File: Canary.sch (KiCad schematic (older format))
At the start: 36 parts, among them J1 CONN_ARM_CM_JTAG_SWD_10, J2 BMD-300-A-R, J3 20021311-00010T4LF, Q1 PMN30UNX, Q2 PMN42XPEAH, Q3 PMN30UNX, SW1 TL3301SPF160QJ, U1 DNP, U2 SHTC3, U3 SGP40, Y1 32.7680 kHz

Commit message: Clean up schem, wire in button
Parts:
- added C26: 0.1u, JetkovKiCADLib:C_0402_NoSilk, symbol Device:C
- added R28: 10k, JetkovKiCADLib:R_0402_NoSilk, symbol Device:R
- added R29: 100k, JetkovKiCADLib:R_0402_NoSilk, symbol Device:R
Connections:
- net labels added: BUTTON
- wire segments 115 -> 127
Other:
- note added: "Button"
- note added: "GPIO Specifications\nVmin = -0.3V, Vmax = VCC+0.3V = 3.9V\nVih = 0.7 * VCC = 2.31V\nVil = 0.3 * VCC = 0.99V"
- note added: "TODO\n- Jellybean BOM\n- Review"
- note removed: "TODO\n- Jellybean BOM\n- Review\n- Button"
- moved on the sheet: C4, J1, U1

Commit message: Spec LED resistors
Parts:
- R10: value ? -> 500R
- R28: value 10k -> 100k
- R8, R9: value ? -> 470R
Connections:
- wire segments 127 -> 132
- no-connect marks 4 -> 9
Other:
- note added: "Vf @ 3mA = 1.8V\nIntensity = 20 mcd"
- note added: "Vf @ 3mA = 1.9V\nIntensity = 20 mcd"
- note added: "Vf @ 3mA = 1.9V\nIntensity = 8 mcd"
- moved on the sheet: C5, Y1
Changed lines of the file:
@@
 L Device:Crystal Y1
 U 1 1 6032C351
-P 5300 1550
-F 0 "Y1" H 5600 1650 50  0000 C CNN
-F 1 "32.7680 kHz" H 5800 1550 50  0000 C CNN
-F 2 "JetkovKiCADLib:FC135327680KAAC3" H 5300 1550 50  0001 C CNN
-F 3 "https://support.epson.biz/td/api/doc_check.php?dl=brief_FC-135&lang=en" H 5300 1550 50  0001 C CNN
-F 4 "CRYSTAL 32.7680KHZ 9PF SMD" H 5300 1550 50  0001 C CNN "Description"
-F 5 "EPSON" H 5300 1550 50  0001 C CNN "Manufacturer"
-F 6 "FC-135 32.7680KA-AC3" H 5300 1550 50  0001 C CNN "Part Number"
-F 7 "-40°C +85°C" H 5300 1550 50  0001 C CNN "Temp Range"
-	1    5300 1550
+P 5350 1550
+F 0 "Y1" H 5650 1650 50  0000 C CNN
+F 1 "32.7680 kHz" H 5850 1550 50  0000 C CNN
+F 2 "JetkovKiCADLib:FC135327680KAAC3" H 5350 1550 50  0001 C CNN
+F 3 "https://support.epson.biz/td/api/doc_check.php?dl=brief_FC-135&lang=en" H 5350 1550 50  0001 C CNN
+F 4 "CRYSTAL 32.7680KHZ 9PF SMD" H 5350 1550 50  0001 C CNN "Description"
+F 5 "EPSON" H 5350 1550 50  0001 C CNN "Manufacturer"
+F 6 "FC-135 32.7680KA-AC3" H 5350 1550 50  0001 C CNN "Part Number"
+F 7 "-40°C +85°C" H 5350 1550 50  0001 C CNN "Temp Range"
+	1    5350 1550
 	1    0    0    -1
 $EndComp
@@
 L Device:C C5
 U 1 1 6032EF01
-P 5100 1750
-F 0 "C5" H 5200 1700 50  0000 L CNN
-F 1 "12pF" H 5200 1800 50  0000 L CNN
-F 2 "JetkovKiCADLib:C_0402_NoSilk" H 5138 1600 50  0001 C CNN
-F 3 "http://www.samsungsem.com/kr/support/product-search/mlcc/__icsFiles/afieldfile/2016/12/14/Data%20sheet_CL05C120JB5NNNC.pdf" H 5100 1750 50  0001 C CNN
-F 4 "CAP CER 12PF 50V C0G/NP0 0402" H 5100 1750 50  0001 C CNN "Description"
-F 5 "Samsung Electro-Mechanics" H 5100 1750 50  0001 C CNN "Manufacturer"
-F 6 "CL05C120JB5NNNC" H 5100 1750 50  0001 C CNN "Part Number"
-F 7 "-55°C +125°C" H 5100 1750 50  0001 C CNN "Temp Range"
-	1    5100 1750
+P 5200 1750
+F 0 "C5" H 5300 1700 50  0000 L CNN
+F 1 "12pF" H 5300 1800 50  0000 L CNN
+F 2 "JetkovKiCADLib:C_0402_NoSilk" H 5238 1600 50  0001 C CNN
+F 3 "http://www.samsungsem.com/kr/support/product-search/mlcc/__icsFiles/afieldfile/2016/12/14/Data%20sheet_CL05C120JB5NNNC.pdf" H 5200 1750 50  0001 C CNN
+F 4 "CAP CER 12PF 50V C0G/NP0 0402" H 5200 1750 50  0001 C CNN "Description"
+F 5 "Samsung Electro-Mechanics" H 5200 1750 50  0001 C CNN "Manufacturer"
+F 6 "CL05C120JB5NNNC" H 5200 1750 50  0001 C CNN "Part Number"
+F 7 "-55°C +125°C" H 5200 1750 50  0001 C CNN "Temp Range"
+	1    5200 1750
 	-1   0    0    1
 $EndComp
 Wire Wire Line
-	5450 1550 5500 1550
-Wire Wire Line
 	5500 1550 5500 1600
 Wire Wire Line
-	5150 1550 5100 1550
-Wire Wire Line
-	5100 1550 5100 1600
+	5200 1550 5200 1600
 $Comp
 L power:GND #PWR023
@@
 L power:GND #PWR021
 U 1 1 60330241
-P 5100 1900
-F 0 "#PWR021" H 5100 1650 50  0001 C CNN
-F 1 "GND" H 5105 1727 50  0000 C CNN
-F 2 "" H 5100 1900 50  0001 C CNN
-F 3 "" H 5100 1900 50  0001 C CNN
-	1    5100 1900
+P 5200 1900
+F 0 "#PWR021" H 5200 1650 50  0001 C CNN
+F 1 "GND" H 5205 1727 50  0000 C CNN
+F 2 "" H 5200 1900 50  0001 C CNN
+F 3 "" H 5200 1900 50  0001 C CNN
+	1    5200 1900
 	-1   0    0    -1
 $EndComp
@@
 Wire Wire Line
 	5500 1350 4450 1350
-Connection ~ 5500 1550
-Wire Wire Line
-	5100 1550 4450 1550
-Connection ~ 5100 1550
 $Comp
 L power:GND #PWR018
@@
 P 5150 6950
 F 0 "R9" H 5220 6996 50  0000 L CNN
-F 1 "?" H 5220 6905 50  0000 L CNN
+F 1 "470R" H 5220 6905 50  0000 L CNN
 F 2 "JetkovKiCADLib:R_0402_NoSilk" V 5080 6950 50  0001 C CNN
 F 3 "~" H 5150 6950 50  0001 C CNN
@@
 P 4600 6950
 F 0 "R8" H 4670 6996 50  0000 L CNN
-F 1 "?" H 4670 6905 50  0000 L CNN
+F 1 "470R" H 4670 6905 50  0000 L CNN
 F 2 "JetkovKiCADLib:R_0402_NoSilk" V 4530 6950 50  0001 C CNN
 F 3 "~" H 4600 6950 50  0001 C CNN
@@
 P 5700 6950
 F 0 "R10" H 5770 6996 50  0000 L CNN
-F 1 "?" H 5770 6905 50  0000 L CNN
+F 1 "500R" H 5770 6905 50  0000 L CNN
 F 2 "JetkovKiCADLib:R_0402_NoSilk" V 5630 6950 50  0001 C CNN
 F 3 "~" H 5700 6950 50  0001 C CNN
@@
 Wire Wire Line
 	1500 2950 1250 2950
-Text GLabel 4500 2850 2    50   Input ~ 0
+Text GLabel 2700 2350 0    50   Input ~ 0
 LED_AMBER
-Text GLabel 4500 2750 2    50   Input ~ 0
+Text GLabel 2700 2250 0    50   Input ~ 0
 LED_RED
-Text GLabel 4500 2950 2    50   Input ~ 0
+Text GLabel 2700 2450 0    50   Input ~ 0
 LED_GREEN
 Text GLabel 4500 3050 2    50   Input ~ 0
@@
 P 1400 5000
 F 0 "R28" H 1470 5046 50  0000 L CNN
-F 1 "10k" H 1470 4955 50  0000 L CNN
+F 1 "100k" H 1470 4955 50  0000 L CNN
 F 2 "JetkovKiCADLib:R_0402_NoSilk" V 1330 5000 50  0001 C CNN
 F 3 "~" H 1400 5000 50  0001 C CNN
@@
 Text Notes 1500 4250 0    79   ~ 0
 Button
+NoConn ~ 2700 1750
+NoConn ~ 2700 1850
+Wire Wire Line
+	2750 1750 2700 1750
+Wire Wire Line
+	2700 1850 2750 1850
+Wire Wire Line
+	4450 1850 4500 1850
+Wire Wire Line
+	4450 1750 4500 1750
+Wire Wire Line
+	2750 2250 2700 2250
+Wire Wire Line
+	2750 2350 2700 2350
+Wire Wire Line
+	2750 2450 2700 2450
+NoConn ~ 4500 1850
+NoConn ~ 4500 2750
+NoConn ~ 4500 2950
+Connection ~ 5500 1550
+Wire Wire Line
+	4450 1550 5200 1550
+Connection ~ 5200 1550
+Text GLabel 4500 1750 2    50   Input ~ 0
+BUTTON
+Text Notes 4200 7700 0    40   ~ 0
+Vf @ 3mA = 1.9V\nIntensity = 8 mcd
+Text Notes 4889 7700 0    40   ~ 0
+Vf @ 3mA = 1.9V\nIntensity = 20 mcd
+Text Notes 5600 7700 0    40   ~ 0
+Vf @ 3mA = 1.8V\nIntensity = 20 mcd
 $EndSCHEMATC

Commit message: Review
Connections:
- no-connect marks 9 -> 10
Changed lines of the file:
@@
 Text Notes 5600 7700 0    40   ~ 0
 Vf @ 3mA = 1.8V\nIntensity = 20 mcd
+NoConn ~ 4500 2850
 $EndSCHEMATC

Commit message: Resolve DRC errors and add proper flagging
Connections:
- net labels added: ~PM_RST~
- net labels removed: PM_nRST
- no-connect marks 10 -> 9
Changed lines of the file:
@@
 	5200 1550 5200 1600
-$Comp
-L power:GND #PWR023
-U 1 1 6032FCEC
-P 5500 1900
-F 0 "#PWR023" H 5500 1650 50  0001 C CNN
-F 1 "GND" H 5505 1727 50  0000 C CNN
-F 2 "" H 5500 1900 50  0001 C CNN
-F 3 "" H 5500 1900 50  0001 C CNN
-	1    5500 1900
-	-1   0    0    -1
-$EndComp
 $Comp
 L power:GND #PWR021
@@
 	-1   0    0    -1
 $EndComp
-Wire Wire Line
-	4450 3550 4500 3550
-Wire Wire Line
-	4500 3550 4500 3600
-$Comp
-L power:+5V #PWR07
-U 1 1 605F5E85
-P 1650 6200
-F 0 "#PWR07" H 1650 6050 50  0001 C CNN
-F 1 "+5V" H 1665 6373 50  0000 C CNN
-F 2 "" H 1650 6200 50  0001 C CNN
-F 3 "" H 1650 6200 50  0001 C CNN
-	1    1650 6200
-	-1   0    0    -1
-$EndComp
 $Comp
 L Device:R R4
@@
 Wire Wire Line
 	2600 6650 2600 6700
-$Comp
-L power:+5V #PWR013
-U 1 1 6066E35F
-P 2600 6200
-F 0 "#PWR013" H 2600 6050 50  0001 C CNN
-F 1 "+5V" H 2615 6373 50  0000 C CNN
-F 2 "" H 2600 6200 50  0001 C CNN
-F 3 "" H 2600 6200 50  0001 C CNN
-	1    2600 6200
-	-1   0    0    -1
-$EndComp
-Wire Wire Line
-	2600 6200 2600 6250
-Wire Wire Line
-	1650 6200 1650 6300
 Wire Wire Line
 	1650 6600 1650 6700
@@
 Wire Wire Line
 	5700 6100 5700 6400
-Wire Wire Line
-	4600 7200 4600 7100
-Wire Wire Line
-	5150 7100 5150 7200
 Wire Wire Line
 	5700 7200 5700 7100
@@
 	7900 3500 7950 3500
 Wire Wire Line
-	7400 3300 7350 3300
-Wire Wire Line
 	7400 3550 7400 3500
 Wire Wire Line
@@
 Text GLabel 7350 3550 0    50   Input ~ 0
 PM_UART_TXD
-Text GLabel 7350 3300 0    50   Input ~ 0
-PM_nRST
-Wire Wire Line
-	7950 3100 7900 3100
-Wire Wire Line
-	7950 3050 7950 3100
-$Comp
-L power:+5V #PWR030
-U 1 1 6031B468
+$Comp
+L power:+5V #PWR028
+U 1 1 603193D6
 P 7950 3050
-F 0 "#PWR030" H 7950 2900 50  0001 C CNN
+F 0 "#PWR028" H 7950 2900 50  0001 C CNN
 F 1 "+5V" H 7965 3223 50  0000 C CNN
 F 2 "" H 7950 3050 50  0001 C CNN
 F 3 "" H 7950 3050 50  0001 C CNN
 	1    7950 3050
-	-1   0    0    -1
-$EndComp
-Wire Wire Line
-	7350 3100 7400 3100
-Wire Wire Line
-	7350 3050 7350 3100
-$Comp
-L power:+5V #PWR028
-U 1 1 603193D6
-P 7350 3050
-F 0 "#PWR028" H 7350 2900 50  0001 C CNN
-F 1 "+5V" H 7365 3223 50  0000 C CNN
-F 2 "" H 7350 3050 50  0001 C CNN
-F 3 "" H 7350 3050 50  0001 C CNN
-	1    7350 3050
 	1    0    0    -1
 $EndComp
@@
 4.4V -> 2.4V\n
 $Comp
-L power:GND #PWR03
-U 1 1 606FE9B8
-P 1350 2000
-F 0 "#PWR03" H 1350 1750 50  0001 C CNN
-F 1 "GND" H 1355 1827 50  0001 C CNN
-F 2 "" H 1350 2000 50  0001 C CNN
-F 3 "" H 1350 2000 50  0001 C CNN
-	1    1350 2000
-	1    0    0    -1
-$EndComp
-$Comp
 L Device:C C1
 U 1 1 606FE9BE
@@
 Wire Wire Line
 	2750 2450 2700 2450
-NoConn ~ 4500 1850
 NoConn ~ 4500 2750
 NoConn ~ 4500 2950
@@
 Vf @ 3mA = 1.8V\nIntensity = 20 mcd
 NoConn ~ 4500 2850
+Wire Wire Line
+	4450 3550 4500 3550
+Wire Wire Line
+	4500 3550 4500 3600
+$Comp
+L power:GND #PWR0101
+U 1 1 606029EA
+P 5500 1900
+F 0 "#PWR0101" H 5500 1650 50  0001 C CNN
+F 1 "GND" H 5505 1727 50  0000 C CNN
+F 2 "" H 5500 1900 50  0001 C CNN
+F 3 "" H 5500 1900 50  0001 C CNN
+	1    5500 1900
+	-1   0    0    -1
+$EndComp
+Wire Wire Line
+	4600 7100 4600 7200
+$Comp
+L power:GND #PWR0102
+U 1 1 60629487
+P 1350 2000
+F 0 "#PWR0102" H 1350 1750 50  0001 C CNN
+F 1 "GND" H 1355 1827 50  0001 C CNN
+F 2 "" H 1350 2000 50  0001 C CNN
+F 3 "" H 1350 2000 50  0001 C CNN
+	1    1350 2000
+	-1   0    0    -1
+$EndComp
+Wire Wire Line
+	5150 7100 5150 7200
+$Comp
+L power:+5V #PWR0103
+U 1 1 6063F55C
+P 2600 6200
+F 0 "#PWR0103" H 2600 6050 50  0001 C CNN
+F 1 "+5V" H 2615 6373 50  0000 C CNN
+F 2 "" H 2600 6200 50  0001 C CNN
+F 3 "" H 2600 6200 50  0001 C CNN
+	1    2600 6200
+	-1   0    0    -1
+$EndComp
+Wire Wire Line
+	2600 6200 2600 6250
+Wire Wire Line
+	7950 3100 7900 3100
+$Comp
+L power:+5V #PWR0104
+U 1 1 606B69D7
+P 7350 3050
+F 0 "#PWR0104" H 7350 2900 50  0001 C CNN
+F 1 "+5V" H 7365 3223 50  0000 C CNN
+F 2 "" H 7350 3050 50  0001 C CNN
+F 3 "" H 7350 3050 50  0001 C CNN
+	1    7350 3050
+	-1   0    0    -1
+$EndComp
+Wire Wire Line
+	7350 3100 7400 3100
+Wire Wire Line
+	7350 3050 7350 3100
+Wire Wire Line
+	7950 3050 7950 3100
+Wire Wire Line
+	7350 3300 7400 3300
+$Comp
+L power:+5V #PWR07
+U 1 1 605F5E85
+P 1650 6200
+F 0 "#PWR07" H 1650 6050 50  0001 C CNN
+F 1 "+5V" H 1665 6373 50  0000 C CNN
+F 2 "" H 1650 6200 50  0001 C CNN
+F 3 "" H 1650 6200 50  0001 C CNN
+	1    1650 6200
+	-1   0    0    -1
+$EndComp
+Wire Wire Line
+	1650 6200 1650 6300
+Text GLabel 4500 1850 2    35   Output ~ 0
+~PM_RST~
+Text GLabel 7350 3300 0    35   Input ~ 0
+~PM_RST~
 $EndSCHEMATC

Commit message: Review everything, ready for layout
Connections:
- net labels added: NG, PG, RBTN
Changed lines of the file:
@@
 Text GLabel 7350 3300 0    35   Input ~ 0
 ~PM_RST~
+Text Label 2300 6450 0    40   ~ 0
+PG
+Text Label 2300 6950 0    40   ~ 0
+NG
+Text Label 1200 4800 0    40   ~ 0
+RBTN
 $EndSCHEMATC

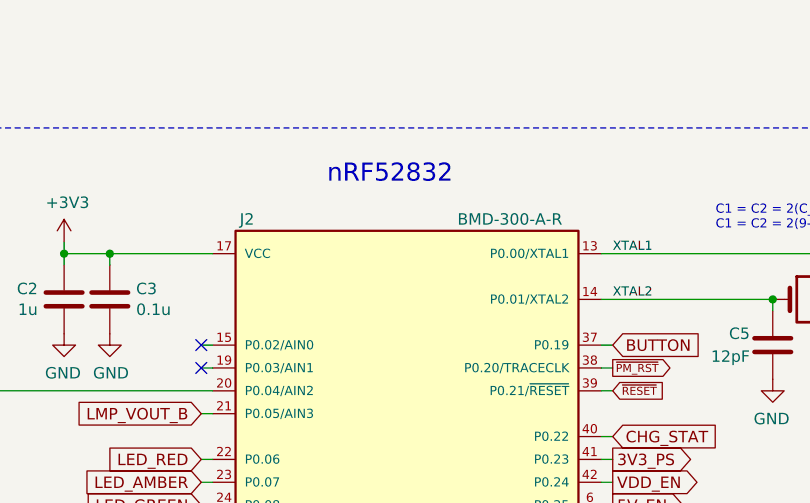
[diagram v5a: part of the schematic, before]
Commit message: Reannotate, fix BMD reference
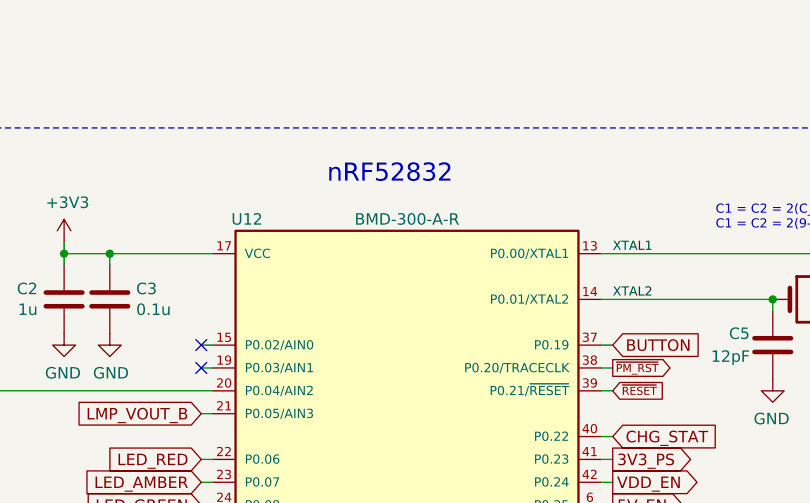
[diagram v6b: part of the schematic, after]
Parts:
- removed J2: BMD-300-A-R, JetkovKiCADLib:BMD-300-A-R, symbol JetkovKiCADLib:BMD-300-A-R
- added U12: BMD-300-A-R, JetkovKiCADLib:BMD-300-A-R, symbol JetkovKiCADLib:BMD-300-A-R
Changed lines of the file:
@@
 $EndDescr
-$Comp
-L JetkovKiCADLib:BMD-300-A-R J2
-U 1 1 60305893
-P 3600 2350
-F 0 "J2" H 2900 3500 50  0000 C CNN
-F 1 "BMD-300-A-R" H 4050 3500 50  0000 C CNN
-F 2 "JetkovKiCADLib:BMD-300-A-R" H 3550 1850 50  0001 L BNN
-F 3 "https://www.u-blox.com/sites/default/files/BMD-300_DataSheet_%28UBX-19033350%29.pdf" H 3600 2350 50  0001 L BNN
-F 4 "BMD-300-A-R" H 3550 1850 50  0001 C CNN "Part Number"
-F 5 "U-Blox" H 3550 1850 50  0001 C CNN "Manufacturer"
-F 6 "RX TXRX MOD BLE 5.0 NORDIC SMD" H 3550 1850 50  0001 C CNN "Description"
-F 7 "-40°C +85°C" H 3650 1750 50  0001 C CNN "Temp Range"
-	1    3600 2350
-	1    0    0    -1
-$EndComp
 $Comp
 L Device:Crystal Y1
@@
 Text Label 1200 4800 0    40   ~ 0
 RBTN
+$Comp
+L JetkovKiCADLib:BMD-300-A-R U12
+U 1 1 6084C612
+P 3600 2350
+F 0 "U12" H 2900 3500 50  0000 C CNN
+F 1 "BMD-300-A-R" H 3600 3500 50  0000 C CNN
+F 2 "JetkovKiCADLib:BMD-300-A-R" H 3550 1650 50  0001 L BNN
+F 3 "https://www.u-blox.com/sites/default/files/BMD-300_DataSheet_%28UBX-19033350%29.pdf" H 3600 2350 50  0001 L BNN
+F 4 "BMD-300-A-R" H 3550 1850 50  0001 C CNN "Part Number"
+F 5 "U-Blox" H 3550 1850 50  0001 C CNN "Manufacturer"
+F 6 "RX TXRX MOD BLE 5.0 NORDIC SMD" H 3550 1850 50  0001 C CNN "Description"
+F 7 "-40°C +85°C" H 3650 1750 50  0001 C CNN "Temp Range"
+	1    3600 2350
+	1    0    0    -1
+$EndComp
 $EndSCHEMATC

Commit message: layout wip
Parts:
- renumbered C9 to C10, C26 to C2, C2 to C3, C3 to C4, C4 to C5, C5 to C6, C6 to C7, C7 to C8, C8 to C9, J3 to J2, R8 to R10, R9 to R11, R10 to R12, R28 to R3, R3 to R4, R29 to R5, R4 to R6, R5 to R7, R6 to R8, R7 to R9, U12 to U1, U1 to U2, U2 to U3, U3 to U4

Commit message: Add resistor details
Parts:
- R1: Description (none) -> RES 2M OHM 1% 1/16W 0402; Manufacturer (none) -> Stackpole Electronics Inc; Part Number (none) -> RMCF0402FT2M00; Temp Range (none) -> -55°C +155°C
- R10, R11: Description (none) -> RES 470 OHM 1% 1/16W 0402; Manufacturer (none) -> Stackpole Electronics Inc; Part Number (none) -> RMCF0402FT470R; Temp Range (none) -> -55°C +155°C
- R12: value 500R -> 499R; Description (none) -> RES 499 OHM 1% 1/16W 0402; Manufacturer (none) -> Stackpole Electronics Inc; Part Number (none) -> RMCF0402FT499R; Temp Range (none) -> -55°C +155°C
- R2: Description (none) -> RES 2.4M OHM 1% 1/16W 0402; Manufacturer (none) -> Stackpole Electronics Inc; Part Number (none) -> RMCF0402FT2M40; Temp Range (none) -> -55°C +155°C
- R3, R5, R6: Description (none) -> RES 100K OHM 1% 1/16W 0402; Manufacturer (none) -> Stackpole Electronics Inc; Part Number (none) -> RMCF0402FT100K; Temp Range (none) -> -55°C +155°C
- R4, R7: Description (none) -> RES 10K OHM 1% 1/16W 0402; Manufacturer (none) -> Stackpole Electronics Inc; Part Number (none) -> RMCF0402FT10K0; Temp Range (none) -> -55°C +155°C
- R8, R9: Description (none) -> RES 100 OHM 1% 1/16W 0402; Manufacturer (none) -> Stackpole Electronics Inc; Part Number (none) -> RMCF0402FT100R; Temp Range (none) -> -55°C +155°C
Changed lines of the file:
@@
 F 1 "100k" H 1720 6405 50  0000 L CNN
 F 2 "JetkovKiCADLib:R_0402_NoSilk" V 1580 6450 50  0001 C CNN
-F 3 "~" H 1650 6450 50  0001 C CNN
+F 3 "https://www.seielect.com/catalog/sei-rmcf_rmcp.pdf" H 1650 6450 50  0001 C CNN
+F 4 "RES 100K OHM 1% 1/16W 0402" H 1650 6450 50  0001 C CNN "Description"
+F 5 "Stackpole Electronics Inc" H 1650 6450 50  0001 C CNN "Manufacturer"
+F 6 "RMCF0402FT100K" H 1650 6450 50  0001 C CNN "Part Number"
+F 7 "-55°C +155°C" H 1650 6450 50  0001 C CNN "Temp Range"
 	1    1650 6450
 	-1   0    0    -1
@@
 F 1 "470R" H 5220 6905 50  0000 L CNN
 F 2 "JetkovKiCADLib:R_0402_NoSilk" V 5080 6950 50  0001 C CNN
-F 3 "~" H 5150 6950 50  0001 C CNN
+F 3 "https://www.seielect.com/catalog/sei-rmcf_rmcp.pdf" H 5150 6950 50  0001 C CNN
+F 4 "RES 470 OHM 1% 1/16W 0402" H 5150 6950 50  0001 C CNN "Description"
+F 5 "Stackpole Electronics Inc" H 5150 6950 50  0001 C CNN "Manufacturer"
+F 6 "RMCF0402FT470R" H 5150 6950 50  0001 C CNN "Part Number"
+F 7 "-55°C +155°C" H 5150 6950 50  0001 C CNN "Temp Range"
 	1    5150 6950
 	1    0    0    -1
@@
 F 1 "470R" H 4670 6905 50  0000 L CNN
 F 2 "JetkovKiCADLib:R_0402_NoSilk" V 4530 6950 50  0001 C CNN
-F 3 "~" H 4600 6950 50  0001 C CNN
+F 3 "https://www.seielect.com/catalog/sei-rmcf_rmcp.pdf" H 4600 6950 50  0001 C CNN
+F 4 "RES 470 OHM 1% 1/16W 0402" H 4600 6950 50  0001 C CNN "Description"
+F 5 "Stackpole Electronics Inc" H 4600 6950 50  0001 C CNN "Manufacturer"
+F 6 "RMCF0402FT470R" H 4600 6950 50  0001 C CNN "Part Number"
+F 7 "-55°C +155°C" H 4600 6950 50  0001 C CNN "Temp Range"
 	1    4600 6950
 	1    0    0    -1
@@
 P 5700 6950
 F 0 "R12" H 5770 6996 50  0000 L CNN
-F 1 "500R" H 5770 6905 50  0000 L CNN
+F 1 "499R" H 5770 6905 50  0000 L CNN
 F 2 "JetkovKiCADLib:R_0402_NoSilk" V 5630 6950 50  0001 C CNN
-F 3 "~" H 5700 6950 50  0001 C CNN
+F 3 "https://www.seielect.com/catalog/sei-rmcf_rmcp.pdf" H 5700 6950 50  0001 C CNN
+F 4 "RES 499 OHM 1% 1/16W 0402" H 5700 6950 50  0001 C CNN "Description"
+F 5 "Stackpole Electronics Inc" H 5700 6950 50  0001 C CNN "Manufacturer"
+F 6 "RMCF0402FT499R" H 5700 6950 50  0001 C CNN "Part Number"
+F 7 "-55°C +155°C" H 5700 6950 50  0001 C CNN "Temp Range"
 	1    5700 6950
 	1    0    0    -1
@@
 F 1 "100R" V 2250 6350 50  0000 L CNN
 F 2 "JetkovKiCADLib:R_0402_NoSilk" V 2080 6450 50  0001 C CNN
-F 3 "~" H 2150 6450 50  0001 C CNN
+F 3 "https://www.seielect.com/catalog/sei-rmcf_rmcp.pdf" H 2150 6450 50  0001 C CNN
+F 4 "RES 100 OHM 1% 1/16W 0402" H 2150 6450 50  0001 C CNN "Description"
+F 5 "Stackpole Electronics Inc" H 2150 6450 50  0001 C CNN "Manufacturer"
+F 6 "RMCF0402FT100R" H 2150 6450 50  0001 C CNN "Part Number"
+F 7 "-55°C +155°C" H 2150 6450 50  0001 C CNN "Temp Range"
 	1    2150 6450
 	0    -1   -1   0
@@
 F 1 "100R" V 2250 6850 50  0000 L CNN
 F 2 "JetkovKiCADLib:R_0402_NoSilk" V 2080 6950 50  0001 C CNN
-F 3 "~" H 2150 6950 50  0001 C CNN
+F 3 "https://www.seielect.com/catalog/sei-rmcf_rmcp.pdf" H 2150 6950 50  0001 C CNN
+F 4 "RES 100 OHM 1% 1/16W 0402" H 2150 6950 50  0001 C CNN "Description"
+F 5 "Stackpole Electronics Inc" H 2150 6950 50  0001 C CNN "Manufacturer"
+F 6 "RMCF0402FT100R" H 2150 6950 50  0001 C CNN "Part Number"
+F 7 "-55°C +155°C" H 2150 6950 50  0001 C CNN "Temp Range"
 	1    2150 6950
 	0    -1   -1   0
@@
 F 1 "10k" H 1770 2605 50  0000 L CNN
 F 2 "JetkovKiCADLib:R_0402_NoSilk" V 1630 2650 50  0001 C CNN
-F 3 "~" H 1700 2650 50  0001 C CNN
+F 3 "https://www.seielect.com/catalog/sei-rmcf_rmcp.pdf" H 1700 2650 50  0001 C CNN
+F 4 "RES 10K OHM 1% 1/16W 0402" H 1700 2650 50  0001 C CNN "Description"
+F 5 "Stackpole Electronics Inc" H 1700 2650 50  0001 C CNN "Manufacturer"
+F 6 "RMCF0402FT10K0" H 1700 2650 50  0001 C CNN "Part Number"
+F 7 "-55°C +155°C" H 1700 2650 50  0001 C CNN "Temp Range"
 	1    1700 2650
 	1    0    0    -1
@@
 F 1 "10k" H 1570 2605 50  0000 L CNN
 F 2 "JetkovKiCADLib:R_0402_NoSilk" V 1430 2650 50  0001 C CNN
-F 3 "~" H 1500 2650 50  0001 C CNN
+F 3 "https://www.seielect.com/catalog/sei-rmcf_rmcp.pdf" H 1500 2650 50  0001 C CNN
+F 4 "RES 10K OHM 1% 1/16W 0402" H 1500 2650 50  0001 C CNN "Description"
+F 5 "Stackpole Electronics Inc" H 1500 2650 50  0001 C CNN "Manufacturer"
+F 6 "RMCF0402FT10K0" H 1500 2650 50  0001 C CNN "Part Number"
+F 7 "-55°C +155°C" H 1500 2650 50  0001 C CNN "Temp Range"
 	1    1500 2650
 	-1   0    0    -1
@@
 F 1 "2.4M" H 1220 1805 50  0000 L CNN
 F 2 "JetkovKiCADLib:R_0402_NoSilk" V 1080 1850 50  0001 C CNN
-F 3 "~" H 1150 1850 50  0001 C CNN
+F 3 "https://www.seielect.com/catalog/sei-rmcf_rmcp.pdf" H 1150 1850 50  0001 C CNN
+F 4 "RES 2.4M OHM 1% 1/16W 0402" H 1150 1850 50  0001 C CNN "Description"
+F 5 "Stackpole Electronics Inc" H 1150 1850 50  0001 C CNN "Manufacturer"
+F 6 "RMCF0402FT2M40" H 1150 1850 50  0001 C CNN "Part Number"
+F 7 "-55°C +155°C" H 1150 1850 50  0001 C CNN "Temp Range"
 	1    1150 1850
 	-1   0    0    -1
@@
 F 1 "2M" H 1220 1405 50  0000 L CNN
 F 2 "JetkovKiCADLib:R_0402_NoSilk" V 1080 1450 50  0001 C CNN
-F 3 "~" H 1150 1450 50  0001 C CNN
+F 3 "https://www.seielect.com/catalog/sei-rmcf_rmcp.pdf" H 1150 1450 50  0001 C CNN
+F 4 "RES 2M OHM 1% 1/16W 0402" H 1150 1450 50  0001 C CNN "Description"
+F 5 "Stackpole Electronics Inc" H 1150 1450 50  0001 C CNN "Manufacturer"
+F 6 "RMCF0402FT2M00" H 1150 1450 50  0001 C CNN "Part Number"
+F 7 "-55°C +155°C" H 1150 1450 50  0001 C CNN "Temp Range"
 	1    1150 1450
 	-1   0    0    1
@@
 F 2 "Mounting_Holes:MountingHole_2.2mm_M2" H 6550 7050 50  0001 C CNN
 F 3 "~" H 6550 7050 50  0001 C CNN
+F 4 "~" H 6550 7050 50  0001 C CNN "Description"
+F 5 "~" H 6550 7050 50  0001 C CNN "Manufacturer"
+F 6 "~" H 6550 7050 50  0001 C CNN "Part Number"
+F 7 "~" H 6550 7050 50  0001 C CNN "Temp Range"
 	1    6550 7050
 	1    0    0    -1
@@
 F 1 "100k" H 1470 4955 50  0000 L CNN
 F 2 "JetkovKiCADLib:R_0402_NoSilk" V 1330 5000 50  0001 C CNN
-F 3 "~" H 1400 5000 50  0001 C CNN
+F 3 "https://www.seielect.com/catalog/sei-rmcf_rmcp.pdf" H 1400 5000 50  0001 C CNN
+F 4 "RES 100K OHM 1% 1/16W 0402" H 1400 5000 50  0001 C CNN "Description"
+F 5 "Stackpole Electronics Inc" H 1400 5000 50  0001 C CNN "Manufacturer"
+F 6 "RMCF0402FT100K" H 1400 5000 50  0001 C CNN "Part Number"
+F 7 "-55°C +155°C" H 1400 5000 50  0001 C CNN "Temp Range"
 	1    1400 5000
 	1    0    0    -1
@@
 F 1 "100k" V 1700 4700 50  0000 L CNN
 F 2 "JetkovKiCADLib:R_0402_NoSilk" V 1530 4800 50  0001 C CNN
-F 3 "~" H 1600 4800 50  0001 C CNN
+F 3 "https://www.seielect.com/catalog/sei-rmcf_rmcp.pdf" H 1600 4800 50  0001 C CNN
+F 4 "RES 100K OHM 1% 1/16W 0402" H 1600 4800 50  0001 C CNN "Description"
+F 5 "Stackpole Electronics Inc" H 1600 4800 50  0001 C CNN "Manufacturer"
+F 6 "RMCF0402FT100K" H 1600 4800 50  0001 C CNN "Part Number"
+F 7 "-55°C +155°C" H 1600 4800 50  0001 C CNN "Temp Range"
 	1    1600 4800
 	0    -1   -1   0
